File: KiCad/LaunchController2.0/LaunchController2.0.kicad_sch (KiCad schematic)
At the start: 40 parts, among them J1 CONN_ICSP, J2 CONN_USB, J3 USB_C_Receptacle_USB2.0_16P, U1 ATmega2560-16A, U2 FT232RNL, U3 USBLC6-2SC6, Y1 HUSG-16.000-20

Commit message: Build-1発行＆発注
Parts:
- removed R7: 10kR, Resistor_SMD:R_0603_1608Metric_Pad0.98x0.95mm_HandSolder, symbol Device:R_Small
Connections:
- net SPI_~{CS}_FeRAM0: no longer names the net of U1.71 (PA7)
- no-connect marks 38 -> 39
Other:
- title: GSE Gen 6 Launch Controller 2.0 -> Gen6 GSE Launch Controller 2.0
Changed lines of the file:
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@@
 	(paper "A4")
 	(title_block
-		(title "GSE Gen 6 Launch Controller 2.0")
+		(title "Gen6 GSE Launch Controller 2.0")
 		(date "2026-03-30")
 	)
@@
 	)
 	(junction
-		(at 116.84 58.42)
-		(diameter 0)
-		(color 0 0 0 0)
-	)
-	(junction
 		(at 15.24 53.34)
 		(diameter 0)
@@
 	)
 	(no_connect
+		(at 90.17 58.42)
+	)
+	(no_connect
 		(at 49.53 76.2)
 	)
@@
 	(wire
 		(pts
-			(xy 116.84 55.88) (xy 116.84 58.42)
-		)
-		(stroke
-			(width 0)
-			(type default)
-		)
-	)
-	(wire
-		(pts
 			(xy 217.17 77.47) (xy 218.44 77.47)
 		)
@@
 	(wire
 		(pts
-			(xy 90.17 58.42) (xy 116.84 58.42)
-		)
-		(stroke
-			(width 0)
-			(type default)
-		)
-	)
-	(wire
-		(pts
 			(xy 69.85 15.24) (xy 72.39 15.24)
 		)
@@
 	(wire
 		(pts
-			(xy 116.84 49.53) (xy 116.84 50.8)
-		)
-		(stroke
-			(width 0)
-			(type default)
-		)
-	)
-	(wire
-		(pts
 			(xy 25.4 132.08) (xy 26.67 132.08)
 		)
@@
 	(wire
 		(pts
-			(xy 116.84 58.42) (xy 121.92 58.42)
-		)
-		(stroke
-			(width 0)
-			(type default)
-		)
-	)
-	(wire
-		(pts
 			(xy 125.73 29.21) (xy 125.73 30.48)
 		)
@@
 		)
 	)
-	(global_label "SPI_~{CS}_FeRAM0"
-		(shape output)
-		(at 121.92 58.42 0)
-		(fields_autoplaced yes)
-		(effects
-			(font
-				(size 1.27 1.27)
-			)
-			(justify left)
-		)
-		(property "Intersheetrefs" "${INTERSHEET_REFS}"
-			(at 139.6009 58.42 0)
-			(effects
-				(font
-					(size 1.27 1.27)
-				)
-				(justify left)
-				(hide yes)
-			)
-		)
-	)
 	(global_label "CTL_IGNITOR"
 		(shape input)
@@
 	)
 	(symbol
-		(lib_id "Device:R_Small")
-		(at 116.84 53.34 0)
-		(unit 1)
-		(exclude_from_sim no)
-		(in_bom yes)
-		(on_board yes)
-		(dnp no)
-		(property "Reference" "R7"
-			(at 119.38 52.705 0)
-			(effects
-				(font
-					(size 1.27 1.27)
-				)
-				(justify left)
-			)
-		)
-		(property "Value" "10kR"
-			(at 119.38 55.245 0)
-			(effects
-				(font
-					(size 1.27 1.27)
-				)
-				(justify left)
-			)
-		)
-		(property "Footprint" "Resistor_SMD:R_0603_1608Metric_Pad0.98x0.95mm_HandSolder"
-			(at 116.84 53.34 0)
-			(effects
-				(font
-					(size 1.27 1.27)
-				)
-				(hide yes)
-			)
-		)
-		(property "Datasheet" "https://www.chip1stop.com/view/dispDetail/DispDetail?partId=ROHM-0021098"
-			(at 116.84 53.34 0)
-			(effects
-				(font
-					(size 1.27 1.27)
-				)
-				(hide yes)
-			)
-		)
-		(property "Description" ""
-			(at 116.84 53.34 0)
-			(effects
-				(font
-					(size 1.27 1.27)
-				)
-			)
-		)
-		(property "LCSC" ""
-			(at 116.84 53.34 0)
-			(effects
-				(font
-					(size 1.27 1.27)
-				)
-				(hide yes)
-			)
-		)
-		(property "Supplier" ""
-			(at 116.84 53.34 0)
-			(effects
-				(font
-					(size 1.27 1.27)
-				)
-				(hide yes)
-			)
-		)
-		(pin "1"
-		)
-		(pin "2"
-		)
-		(instances
-			(project "LaunchController2.0"
-				(path "/017c5872-fa6f-4200-9242-8d168e4d6b79"
-					(reference "R7")
-					(unit 1)
-				)
-			)
-		)
-	)
-	(symbol
 		(lib_id "Device:C_Small")
 		(at 21.59 53.34 90)
@@
 					(unit 1)
 				)
-			)
-		)
-	)
-	(symbol
-		(lib_id "power:+5V")
-		(at 116.84 49.53 0)
-		(unit 1)
-		(exclude_from_sim no)
-		(in_bom yes)
-		(on_board yes)
-		(dnp no)
-		(fields_autoplaced yes)
-		(property "Reference" "#PWR07"
-			(at 116.84 53.34 0)
-			(effects
-				(font
-					(size 1.27 1.27)
-				)
-				(hide yes)
-			)
-		)
-		(property "Value" "+5V"
-			(at 116.84 45.72 0)
-			(effects
-				(font
-					(size 1.27 1.27)
-				)
-			)
-		)
-		(property "Footprint" ""
-			(at 116.84 49.53 0)
-			(effects
-				(font
-					(size 1.27 1.27)
-				)
-				(hide yes)
-			)
-		)
-		(property "Datasheet" ""
-			(at 116.84 49.53 0)
-			(effects
-				(font
-					(size 1.27 1.27)
-				)
-				(hide yes)
-			)
-		)
-		(property "Description" ""
-			(at 116.84 49.53 0)
-			(effects
-				(font
-					(size 1.27 1.27)
-				)
-			)
-		)
-		(pin "1"
-		)
-		(instances
-			(project "LaunchController2.0"
-				(path "/017c5872-fa6f-4200-9242-8d168e4d6b79"
-					(reference "#PWR07")
-					(unit 1)
-				)

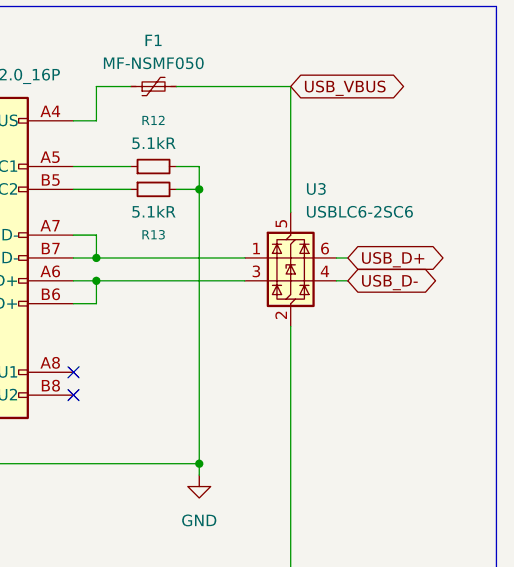
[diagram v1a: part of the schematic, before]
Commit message: USB＋，USB－の配線を修正
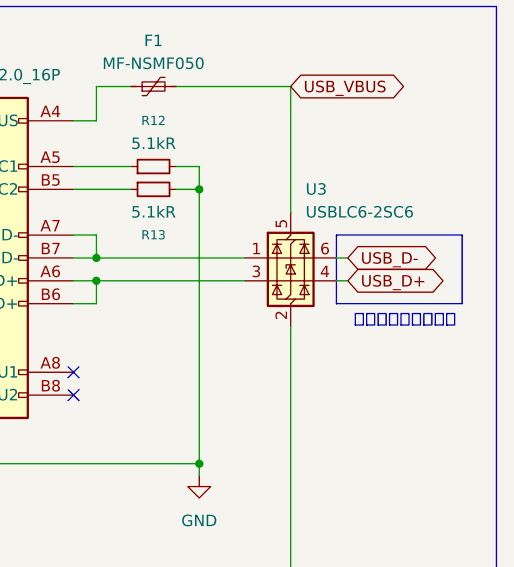
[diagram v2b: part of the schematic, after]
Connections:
- net USB_D+: now also U3.4 (I/O2); no longer U3.6 (I/O1)
- net USB_D-: now also U3.6 (I/O1); no longer U3.4 (I/O2)
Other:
- note added: "向きに気をつけよう"
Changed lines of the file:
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@@
 		)
 	)
+	(rectangle
+		(start 262.89 39.37)
+		(end 276.86 46.99)
+		(stroke
+			(width 0)
+			(type default)
+		)
+		(fill
+			(type none)
+		)
+	)
 	(text "CONNECTION ICSP"
 		(exclude_from_sim no)
@@
 		)
 	)
+	(text "向きに気をつけよう"
+		(exclude_from_sim no)
+		(at 270.51 49.022 0)
+		(effects
+			(font
+				(size 1.27 1.27)
+			)
+		)
+	)
 	(text "CONNECTION USB"
 		(exclude_from_sim no)
@@
 		)
 	)
+	(global_label "USB_D-"
+		(shape bidirectional)
+		(at 264.16 41.91 0)
+		(fields_autoplaced yes)
+		(effects
+			(font
+				(size 1.27 1.27)
+			)
+			(justify left)
+		)
+		(property "Intersheetrefs" "${INTERSHEET_REFS}"
+			(at 275.8765 41.91 0)
+			(effects
+				(font
+					(size 1.27 1.27)
+				)
+				(justify left)
+				(hide yes)
+			)
+		)
+	)
 	(global_label "VREF_THERMISTOR"
 		(shape input)
@@
 		)
 	)
+	(global_label "USB_D+"
+		(shape bidirectional)
+		(at 264.16 44.45 0)
+		(fields_autoplaced yes)
+		(effects
+			(font
+				(size 1.27 1.27)
+			)
+			(justify left)
+		)
+		(property "Intersheetrefs" "${INTERSHEET_REFS}"
+			(at 275.8765 44.45 0)
+			(effects
+				(font
+					(size 1.27 1.27)
+				)
+				(justify left)
+				(hide yes)
+			)
+		)
+	)
 	(global_label "LED_FB_OPEN"
 		(shape output)
@@
 		)
 	)
-	(global_label "USB_D-"
-		(shape bidirectional)
-		(at 264.16 44.45 0)
-		(fields_autoplaced yes)
-		(effects
-			(font
-				(size 1.27 1.27)
-			)
-			(justify left)
-		)
-		(property "Intersheetrefs" "${INTERSHEET_REFS}"
-			(at 275.8765 44.45 0)
-			(effects
-				(font
-					(size 1.27 1.27)
-				)
-				(justify left)
-				(hide yes)
-			)
-		)
-	)
 	(global_label "LED_FB_PURGE"
 		(shape output)
@@
 			(effects
 				(font
-					(size 1.27 1.27)
-				)
-				(justify left)
-				(hide yes)
-			)
-		)
-	)
-	(global_label "USB_D+"
-		(shape bidirectional)
-		(at 264.16 41.91 0)
-		(fields_autoplaced yes)
-		(effects
-			(font
-				(size 1.27 1.27)
-			)
-			(justify left)
-		)
-		(property "Intersheetrefs" "${INTERSHEET_REFS}"
-			(at 275.8765 41.91 0)
-			(effects
-				(font
